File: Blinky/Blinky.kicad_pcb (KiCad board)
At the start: 2 copper layers, 41.1 x 64.6 mm, 69 parts, among them J1 Conn_01x06_Socket, J2 Conn_01x06_Socket, J3 Battery Connector, J4 Charging Notches, Q1 IRLML6244, Q2 IRLML6244, Q3 IRLML6244, Q4 IRLML6244, Q5 IRLML6244, Q6 IRLML6244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

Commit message: cosmetics
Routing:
- net Net-(U4B-IN2-): track 48.3 -> 42.8 mm
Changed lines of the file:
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@@
   (via (at 133.7 98.3) (size 0.8) (drill 0.4) (layers "F.Cu" "B.Cu") (net 58))
   (segment (start 154.8 98.3) (end 133.7 98.3) (width 0.25) (layer "B.Cu") (net 58))
-  (segment (start 127.675 96.55) (end 127.45 96.325) (width 0.25) (layer "F.Cu") (net 59))
   (segment (start 157.2 86.7) (end 154.4 89.5) (width 0.25) (layer "F.Cu") (net 59))
-  (segment (start 127.45 96.325) (end 127.45 94.55) (width 0.25) (layer "F.Cu") (net 59))
   (segment (start 154.4 89.5) (end 154.2 89.5) (width 0.25) (layer "F.Cu") (net 59))
   (segment (start 151 92.5) (end 151.1 92.6) (width 0.25) (layer "F.Cu") (net 59))
-  (segment (start 129.675 97) (end 129.225 96.55) (width 0.25) (layer "F.Cu") (net 59))
   (segment (start 160.460001 88.525) (end 160.635001 88.7) (width 0.25) (layer "F.Cu") (net 59))
   (segment (start 160.635001 88.7) (end 160.635001 88.435001) (width 0.25) (layer "F.Cu") (net 59))
+  (segment (start 130.487726 96.330497) (end 130.344503 96.330497) (width 0.25) (layer "F.Cu") (net 59))
   (segment (start 160.635001 88.435001) (end 158.8 86.6) (width 0.25) (layer "F.Cu") (net 59))
-  (segment (start 129.225 96.55) (end 127.675 96.55) (width 0.25) (layer "F.Cu") (net 59))
-  (segment (start 127.45 94.55) (end 128.7 93.3) (width 0.25) (layer "F.Cu") (net 59))
   (segment (start 148.9 92.5) (end 151 92.5) (width 0.25) (layer "F.Cu") (net 59))
   (segment (start 160.635001 92.327584) (end 160.635001 88.7) (width 0.25) (layer "F.Cu") (net 59))
+  (segment (start 130.344503 96.330497) (end 129.675 97) (width 0.25) (layer "F.Cu") (net 59))
   (segment (start 129.675 98.5) (end 129.675 97) (width 0.25) (layer "F.Cu") (net 59))
   (segment (start 159.4 88.525) (end 160.460001 88.525) (width 0.25) (layer "F.Cu") (net 59))
@@
   (via (at 148.9 92.5) (size 0.8) (drill 0.4) (layers "F.Cu" "B.Cu") (net 59))
   (via (at 154.2 89.5) (size 0.8) (drill 0.4) (layers "F.Cu" "B.Cu") (net 59))
-  (via (at 128.7 93.3) (size 0.8) (drill 0.4) (layers "F.Cu" "B.Cu") (net 59))
   (via (at 151.1 92.6) (size 0.8) (drill 0.4) (layers "F.Cu" "B.Cu") (net 59))
+  (via (at 130.487726 96.330497) (size 0.8) (drill 0.4) (layers "F.Cu" "B.Cu") (net 59))
   (via (at 157.2 86.7) (size 0.8) (drill 0.4) (layers "F.Cu" "B.Cu") (net 59))
-  (segment (start 128.7 93.3) (end 148.1 93.3) (width 0.25) (layer "B.Cu") (net 59))
+  (segment (start 130.487726 96.330497) (end 130.669503 96.330497) (width 0.25) (layer "B.Cu") (net 59))
   (segment (start 148.1 93.3) (end 148.9 92.5) (width 0.25) (layer "B.Cu") (net 59))
+  (segment (start 133.7 93.3) (end 148.1 93.3) (width 0.25) (layer "B.Cu") (net 59))
   (segment (start 158.8 86.6) (end 157.3 86.6) (width 0.25) (layer "B.Cu") (net 59))
   (segment (start 154.2 89.5) (end 151.1 92.6) (width 0.25) (layer "B.Cu") (net 59))
+  (segment (start 130.669503 96.330497) (end 133.7 93.3) (width 0.25) (layer "B.Cu") (net 59))
   (segment (start 157.3 86.6) (end 157.2 86.7) (width 0.25) (layer "B.Cu") (net 59))
   (segment (start 135.149936 83.050051) (end 135.149936 84.284938) (width 0.25) (layer "F.Cu") (net 60))

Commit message: trying to fix C5
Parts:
- C1: value 1uf -> 47uf
- C5: value 470uf -> 1000uf; footprint Capacitor_SMD:C_0603_1608Metric -> footprint:CAP-SMD_BD8.0-L8.3-W8.3-FD
- C6: value 100uF -> 10uf
- C8: value 1uf -> 100nf
- moved C5 19.5 mm to (175.2, 65.9)
- moved C11 4.21 mm to (127.9, 92.4)
- moved R34 3.96 mm to (130.9, 98.9), turned to 180 degrees
- moved U3 3.61 mm to (143.9, 95.5)
- moved R31 3.24 mm to (127.8, 77.0)
- moved R27 2.64 mm to (128.1, 95.9), turned to 90 degrees
- moved R28 2.62 mm to (127.9, 98.2)
- moved C4 2.60 mm to (127.9, 99.9)
- moved U7 2.42 mm to (129.0, 104.4)
- moved C8 1.98 mm to (159.3, 58.5), turned to -90 degrees
- moved R25 1.61 mm to (155.7, 98.4)
- moved R29 1.60 mm to (127.6, 101.6)
- moved R32 1.40 mm to (131.2, 101.8)
- moved U10 1.33 mm to (157.7, 61.0)
- moved R5 1.24 mm to (155.6, 59.3), turned to 90 degrees
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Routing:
- net /USB-: track 42.6 -> 54.7 mm
- net CHARGE+: track 54.3 -> 66.4 mm
- net Net-(U4B-OUT2): track 36.0 -> 42.6 mm, vias 5 -> 4
- net /MIC: track 13.0 -> 6.39 mm
- net GND: track 269.5 -> 276.1 mm, vias 18 -> 16
- net Net-(U4B-IN2-): track 42.8 -> 48.7 mm
- net /USB+: track 45.8 -> 51.1 mm
- net Net-(C11-Pad1): track 8.28 -> 13.5 mm
- net /PIN8: track 14.3 -> 18.9 mm, vias 2 -> 0
- net Net-(U4A-IN1-): track 31.2 -> 35.7 mm
- net /EN: track 20.9 -> 24.8 mm
- net /PIN32: track 9.08 -> 12.8 mm
- net /GREEN2: track 52.2 -> 55.8 mm
- net /BOOT: track 6.55 -> 10.2 mm
- net /PIN34: track 6.18 -> 9.77 mm
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- added copper zone on F.Cu, net (none)
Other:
- board size 41.1 x 64.6 mm -> 43.1 x 64.6 mm

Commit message: reordered
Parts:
- moved C5 29.1 mm to (150.0, 80.5), turned to 180 degrees
- moved C8 16.6 mm to (166.4, 73.5), turned to 90 degrees
- moved BOOT 11.3 mm to (134.3, 67.9)
- moved R31 8.31 mm to (127.5, 68.7)
- moved RESET 6.75 mm to (139.3, 82.1)
- moved Q6 5.45 mm to (129.4, 54.2)
- moved C9 5.35 mm to (135.9, 77.3), turned to 180 degrees
- moved R12 4.81 mm to (128.6, 57.2)
- moved Q5 4.72 mm to (129.4, 50.6)
- moved R17 4.26 mm to (128.4, 61.7)
- moved R18 4.26 mm to (128.4, 59.9)
- moved R16 4.24 mm to (128.5, 63.4)
- moved Q4 4.11 mm to (129.2, 47.1)
- moved R7 3.35 mm to (132.8, 48.0)
- moved R11 2.93 mm to (134.2, 58.9)
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- renumbered U11 to BOOT, U15 to RESET
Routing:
- net VDD: track 137.6 -> 166.2 mm, vias 9 -> 10
- net Net-(U11-B): track 6.54 -> 21.2 mm, vias 0 -> 2
- net /BOOT: track 10.2 -> 23.1 mm, vias 0 -> 2
- net GND: track 276.1 -> 288.3 mm, vias 16 -> 18
- net Net-(U15-B): track 9.80 -> 18.4 mm
- net /GREEN2: track 55.8 -> 64.0 mm
- net /BLUE1: track 60.5 -> 68.2 mm
- net /GREEN1: track 56.3 -> 62.0 mm
- net /BLUE2: track 53.0 -> 58.3 mm
- net Net-(Q5-D): track 18.3 -> 23.2 mm
- net /USB-: track 54.7 -> 49.8 mm
- net Net-(Q6-D): track 16.4 -> 20.5 mm
- net /RED1: track 41.3 -> 45.1 mm
- net Net-(Q5-G): track 9.84 -> 12.2 mm
- net Net-(Q4-G): track 9.14 -> 11.4 mm
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
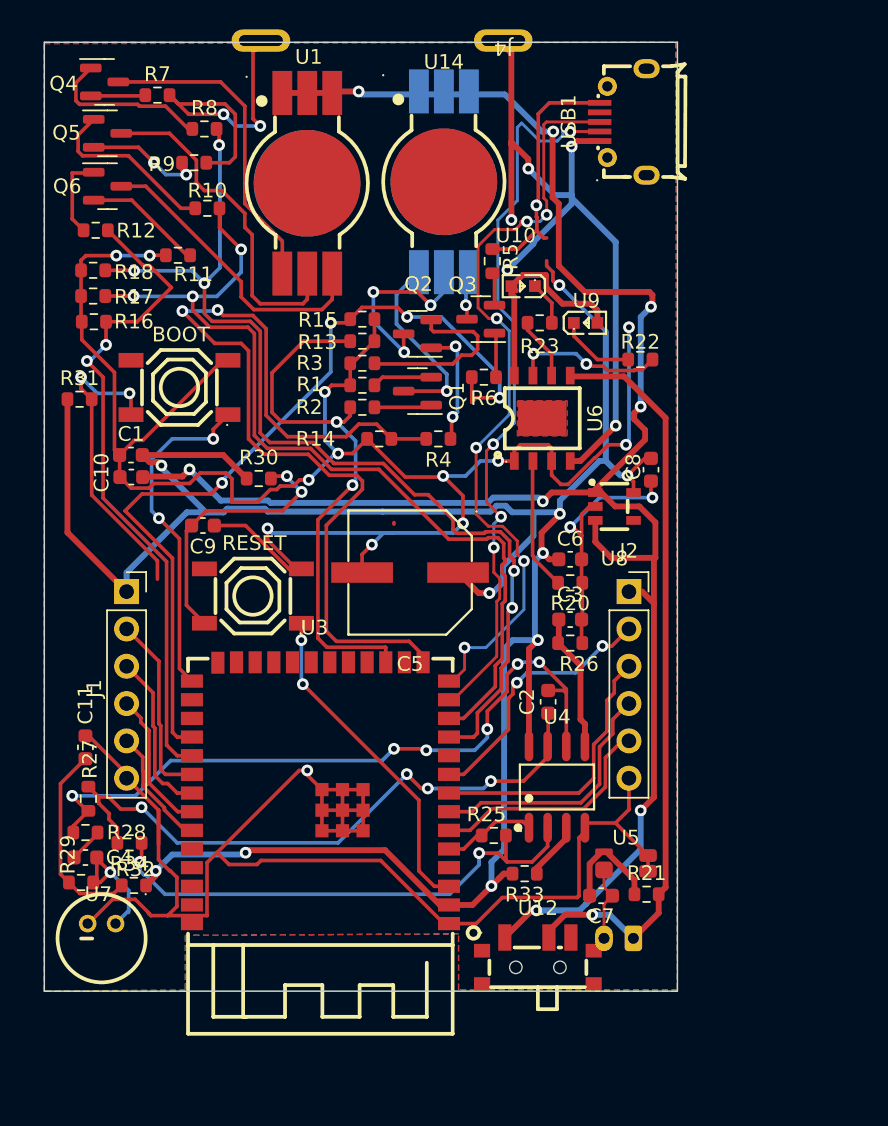
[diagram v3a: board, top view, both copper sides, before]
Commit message: reordered and fixed stuff
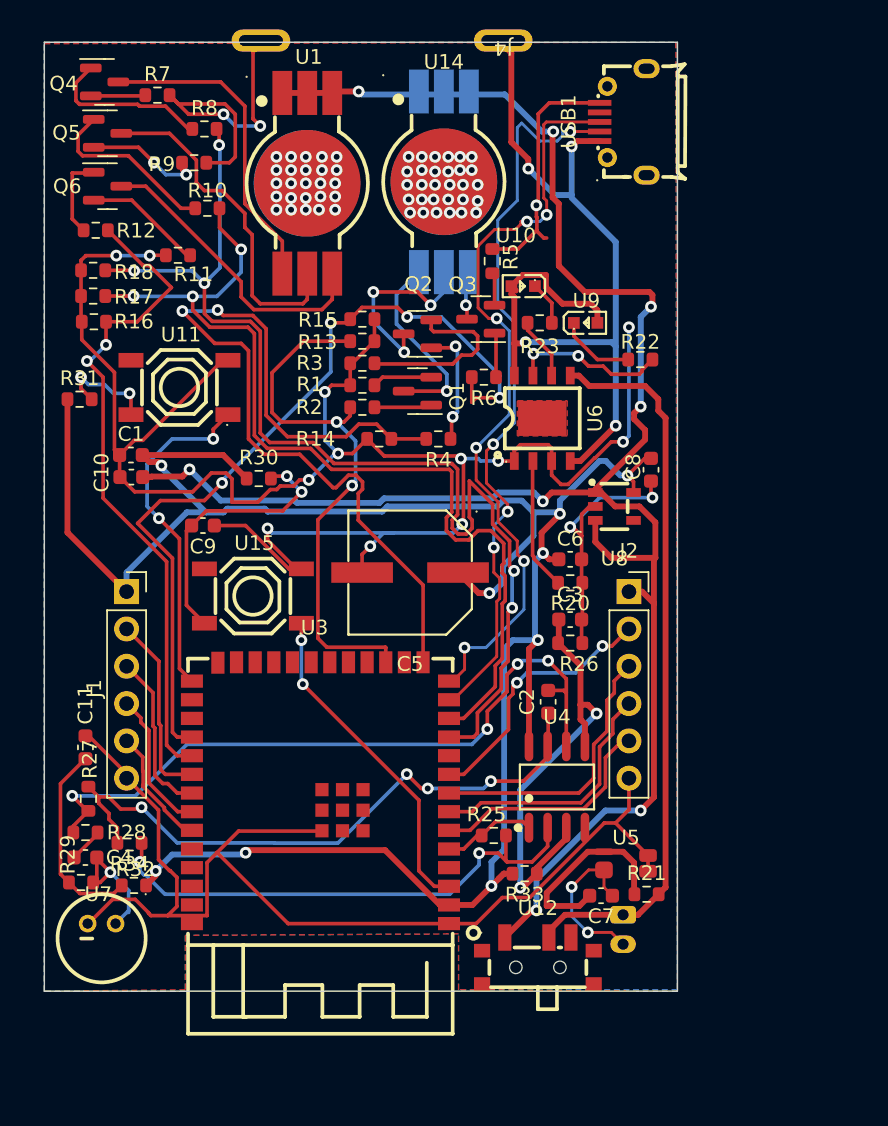
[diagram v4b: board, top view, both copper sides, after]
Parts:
- C5: footprint footprint:CAP-SMD_BD8.0-L8.3-W8.3-FD -> footprint6:CAP-SMD_BD8.0-L8.3-W8.3-FD
- moved J3 1.75 mm to (164.5, 103.8), turned to -90 degrees
- renumbered BOOT to U11, RESET to U15
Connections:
- U1 pad 7: unconnected-(U1-Pad7) -> /LED1
- U13 pad 7: unconnected-(U13-Pad7) -> /LED1
- U14 pad 7: unconnected-(U14-Pad7) -> /LED2
- U2 pad 7: unconnected-(U2-Pad7) -> /LED2
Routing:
- net GND: track 288.3 -> 263.7 mm, vias 18 -> 17
- net /VDD_REF: track 13.4 -> 30.2 mm, vias 0 -> 2
- net VDD: track 166.2 -> 149.7 mm, vias 10 -> 9
- net Net-(U11-B): track 21.2 -> 7.05 mm
- net /BLUE1: track 68.2 -> 76.5 mm
- net Net-(U5-VDD): track 7.33 -> 13.7 mm
- net /BAT-: track 5.13 -> 11.0 mm, vias 0 -> 2
- net CHARGE+: track 66.4 -> 61.2 mm, vias 5 -> 4
- net /GREEN2: track 64.0 -> 60.0 mm
- net /GREEN1: track 62.0 -> 65.2 mm
- net /BLUE2: track 58.3 -> 56.6 mm
- net /BAT+: track 51.3 -> 49.7 mm, vias 1 -> 0
- net /USB+: track 52.7 -> 52.0 mm
- net Net-(U4B-IN2-): track 48.6 -> 48.7 mm, vias 6 -> 4
- net /LED2: vias 0 -> 30
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
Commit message: removed some violations
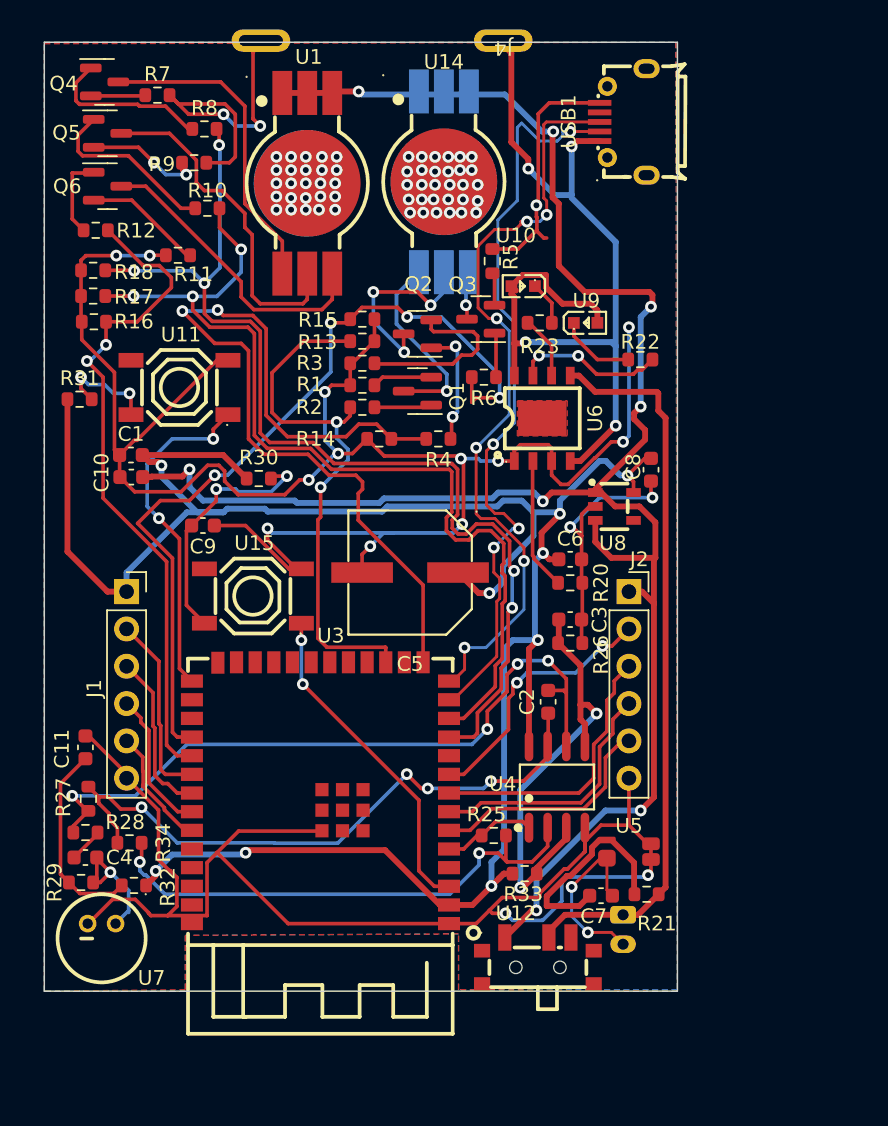
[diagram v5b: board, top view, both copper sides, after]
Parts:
- moved U5 0.82 mm to (164.9, 99.5)
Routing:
- net GND: track 263.7 -> 279.1 mm, vias 17 -> 19
- net /BLUE1: track 76.5 -> 71.2 mm
- net Net-(U15-B): track 18.4 -> 17.0 mm
- net /BAT-: track 11.0 -> 12.2 mm
- net /USB-: track 50.2 -> 51.4 mm
- net VDD: track 149.7 -> 150.8 mm
- net Net-(U5-VDD): track 13.7 -> 14.5 mm
- net VBAT: track 131.7 -> 132.4 mm
- net /GREEN2: track 60.0 -> 59.3 mm
- net /USB+: track 52.0 -> 52.5 mm

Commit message: review by blueloop
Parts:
- removed U13, U14: XL-HD6070RGBC-A46L, footprint:LED-SMD_XL-HD6070RGBC-A46L-BACKSIDE
- added C12: 100nF, Capacitor_SMD:C_0603_1608Metric, F.Cu at (152.4, 74.3)
- added R19: 470k, Resistor_SMD:R_0603_1608Metric, F.Cu at (150.0, 74.3)
- added R24: 470k, Resistor_SMD:R_0603_1608Metric, F.Cu at (147.5, 74.3)
- LED1: renamed from U1; footprint footprint:LED-SMD_XL-HD6070RGBC-A46L -> Library:LED-SMD_XL-HD6070RGBC-A46L
- LED2: renamed from U2; footprint footprint:LED-SMD_XL-HD6070RGBC-A46L -> Library:LED-SMD_XL-HD6070RGBC-A46L
- moved C7 0.40 mm to (163.0, 102.1)
- moved R21 0.30 mm to (166.1, 102.1)
- renumbered U7 to MIC1, U12 to SW1, U11 to T1, U15 to T2
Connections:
- U3 pad 4: unconnected-(U3-IO4-Pad4) -> /VBAT_MESS
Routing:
- net /VBAT_MESS: track 0.00 -> 39.2 mm, vias 0 -> 6
- net /GREEN2: track 59.3 -> 23.6 mm
- net VBAT: track 132.4 -> 152.8 mm, vias 8 -> 6
- net VDD: track 150.8 -> 143.8 mm, vias 9 -> 8
- net CHARGE+: track 61.2 -> 54.2 mm, vias 4 -> 5
- net /RED2: track 37.0 -> 30.1 mm
- net /GREEN1: track 65.2 -> 59.8 mm
- net /BLUE1: track 71.2 -> 66.0 mm
- net Net-(U5-VDD): track 14.5 -> 9.86 mm
- net GND: track 279.1 -> 283.2 mm, vias 19 -> 67
- net /USB+: track 52.5 -> 49.9 mm, vias 6 -> 4
- net /RED1: track 45.5 -> 43.4 mm
- net /USB-: track 51.4 -> 49.7 mm
- net /BAT-: track 12.2 -> 10.8 mm
- net Net-(U4B-OUT2): track 43.5 -> 44.8 mm
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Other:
- board size 43.1 x 64.6 mm -> 43 x 64.5 mm

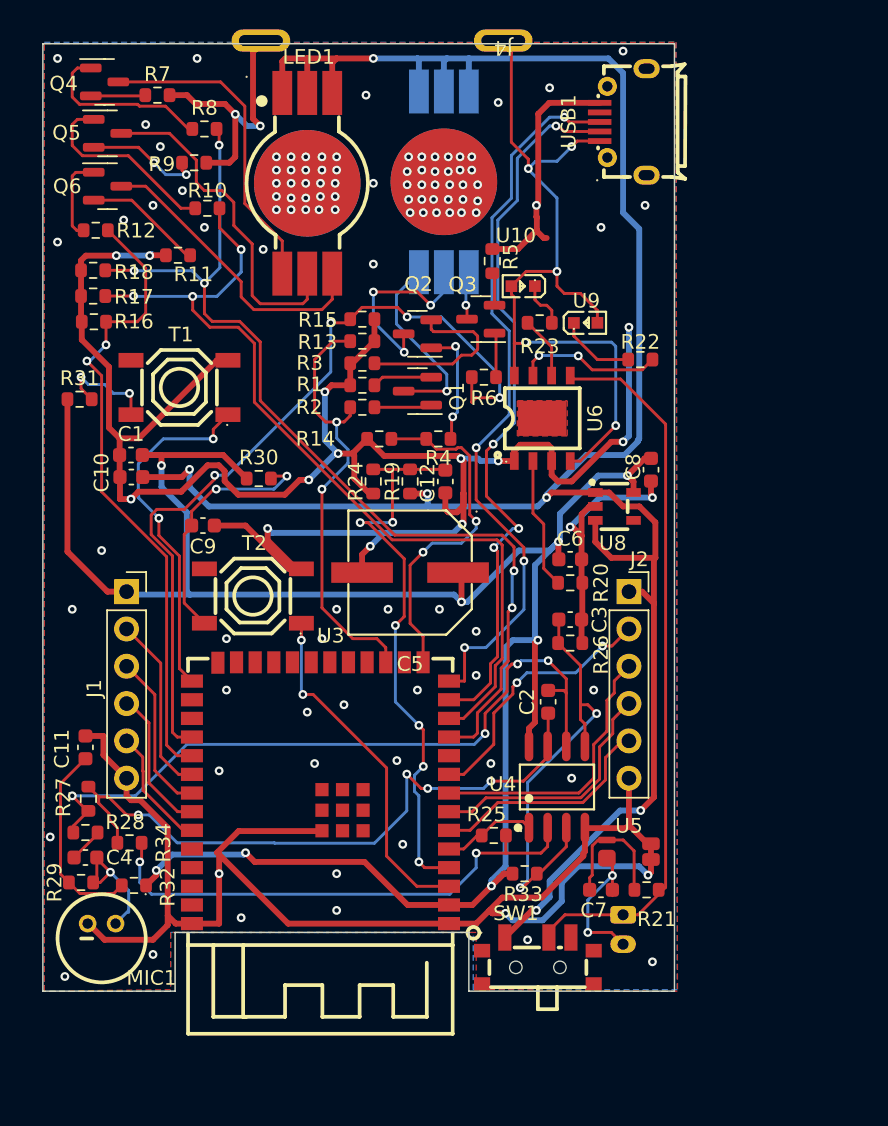
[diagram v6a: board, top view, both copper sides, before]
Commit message: 3d work and fixed 90 deg rotation in capacitor issue
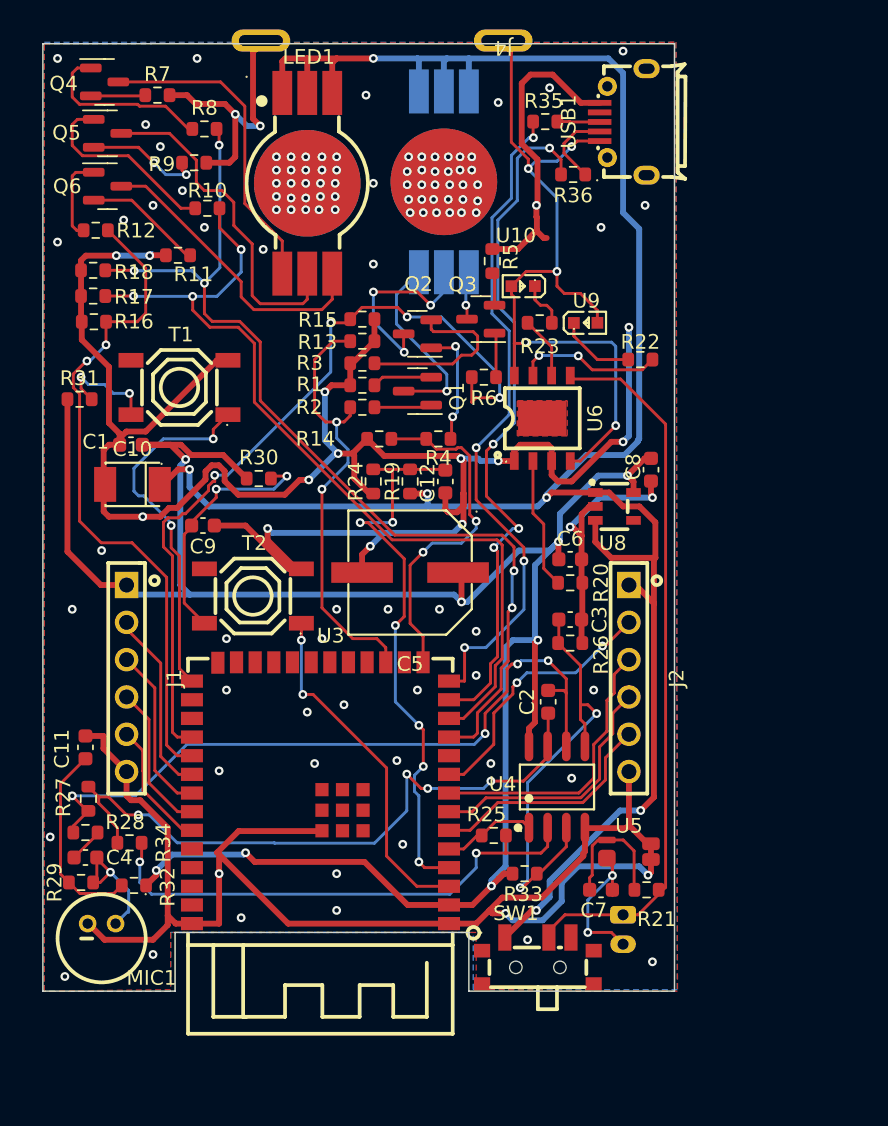
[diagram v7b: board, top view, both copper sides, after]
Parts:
- added R35: 10, Resistor_SMD:R_0603_1608Metric, F.Cu at (159.2, 49.8)
- added R36: 10, Resistor_SMD:R_0603_1608Metric, F.Cu at (161.1, 53.4)
- C10: footprint Capacitor_SMD:C_0603_1608Metric -> footprint:CASE-B_3528
- J1, J2: footprint Connector_PinSocket_2.54mm:PinSocket_1x06_P2.54mm_Vertical -> footprint:HDR-TH_6P-P2.54-V-F
- moved J1 5.90 mm to (130.7, 87.7), turned to -90 degrees
- moved J2 5.90 mm to (164.9, 87.7), turned to -90 degrees
- moved C1 0.70 mm to (131.0, 71.8)
- moved C10 0.51 mm to (131.1, 74.5), turned to 180 degrees
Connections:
- C10 pad 1: GND -> VBAT
- C10 pad 2: VBAT -> GND
- USB1 pad 2: /USB- -> Net-(USB1-D-)
- USB1 pad 3: /USB+ -> Net-(USB1-D+)
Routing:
- net GND: track 283.2 -> 291.8 mm
- net Net-(USB1-D-): track 0.00 -> 5.48 mm
- net /USB+: track 49.9 -> 45.8 mm
- net Net-(USB1-D+): track 0.00 -> 2.94 mm
- net VDD: track 143.8 -> 146.1 mm
- net /USB-: track 49.7 -> 47.6 mm
- net /RED1: track 43.4 -> 45.4 mm
- net /BLUE2: track 55.7 -> 54.5 mm
- net VBAT: track 152.8 -> 151.6 mm
- net /PIN7: track 17.1 -> 18.0 mm
- net /PIN34: track 9.89 -> 10.7 mm
- net /PIN6: track 15.7 -> 16.3 mm

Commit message: casing update
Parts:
- added C13: 18pf, Capacitor_SMD:C_0603_1608Metric, F.Cu at (142.9, 87.3)
- added C14: 18pf, Capacitor_SMD:C_0603_1608Metric, F.Cu at (135.2, 87.3)
- added TXAL1: Q13FC1350000400, footprint3:FC-135R_L3.2-W1.5, F.Cu at (138.9, 87.5)
- moved USB1 57.3 mm to (156.4, 106.5), turned to 0 degrees
- moved R35 53.1 mm to (159.4, 102.9), turned to 0 degrees
- moved R36 49.8 mm to (156.1, 102.9)
- moved SW1 6.60 mm to (165.3, 106.9)
- moved J3 5.10 mm to (164.6, 98.7)
- moved U3 4.54 mm to (142.0, 99.6)
- moved U5 2.91 mm to (165.1, 96.6)
- moved J1 2.30 mm to (128.4, 87.7)
- moved R27 1.90 mm to (126.2, 95.8)
- moved C11 1.70 mm to (126.2, 92.5)
- moved R34 1.48 mm to (129.6, 98.2), turned to 90 degrees
- moved R32 1.26 mm to (130.0, 101.4)
- moved C4 1.00 mm to (126.9, 99.9)
- moved R28 1.00 mm to (126.9, 98.2)
- moved R29 0.81 mm to (126.8, 101.5)
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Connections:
- J1 pad 2: /PIN32 -> /PIN37
- J1 pad 3: /PIN33 -> /PIN36
- U3 pad 10: /PIN10 -> /BLUE1
- U3 pad 11: /BLUE1 -> unconnected-(U3-IO18-Pad11)
- U3 pad 32: /PIN32 -> /32_32khz
- U3 pad 33: /PIN33 -> /33_32khz
- U3 pad 36: unconnected-(U3-RXD0-Pad36) -> /PIN36
- U3 pad 37: unconnected-(U3-TXD0-Pad37) -> /PIN37
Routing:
- net GND: track 291.8 -> 212.8 mm, vias 67 -> 59
- net CHARGE+: track 54.2 -> 108.3 mm, vias 5 -> 6
- net /USB-: track 47.6 -> 19.0 mm
- net /PIN37: track 0.00 -> 26.1 mm, vias 0 -> 2
- net /PIN36: track 0.00 -> 21.6 mm, vias 0 -> 2
- net /33_32khz: track 0.00 -> 18.9 mm, vias 0 -> 2
- net /USB+: track 45.8 -> 27.2 mm, vias 4 -> 2
- net /32_32khz: track 0.00 -> 14.7 mm, vias 0 -> 2
- net /PIN32: track 12.7 -> 0.00 mm
- net /PIN33: track 11.5 -> 0.00 mm
- net /MIC: track 6.39 -> 12.5 mm
- net /BLUE1: track 66.0 -> 72.0 mm
- net /GREEN1: track 59.8 -> 65.6 mm
- net /BOOT: track 24.6 -> 30.0 mm
- net /PIN9: track 18.1 -> 23.4 mm
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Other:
- board size 43 x 64.5 mm -> 44.9 x 64.5 mm
